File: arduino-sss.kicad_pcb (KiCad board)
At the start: 2 copper layers, 68.6 x 53.3 mm, 47 parts, among them J1 Conn_01x03_Male, J2 Barrel_Jack_Switch, J3 DB9_Male, J4 Conn_01x02_Male, J5 Conn_02x03_Odd_Even, P1 Power, P2 Analog, P3 Digital, P4 Digital, P5 CONN_01X01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

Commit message: update
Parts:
- J3: value DB9_Male -> DB9_Female_MountingHoles; footprint Connector_Dsub:DSUB-9_Male_Horizontal_P2.77x2.54mm_EdgePinOffset9.40mm -> Connector_Dsub:DSUB-9_Female_Horizontal_P2.77x2.84mm_EdgePinOffset4.94mm_Housed_MountingHolesOffset7.48mm
- moved J1 66.7 mm to (113.4, 111.4), turned to 90 degrees
- moved SW1 56.1 mm to (165.6, 96.9), turned to 180 degrees
- moved C1 53.9 mm to (121.5, 104.9), turned to 270 degrees
- moved R7 50.8 mm to (131.6, 87.2), turned to 0 degrees
- moved C3 46.1 mm to (129.5, 109.5), turned to 0 degrees
- moved R9 42.7 mm to (167.7, 110.6), turned to 270 degrees
- moved C9 38.8 mm to (151.6, 119.8), turned to 0 degrees
- moved R2 38.1 mm to (138.9, 110.6), turned to 0 degrees
- moved R11 37.6 mm to (172.0, 110.6), turned to 270 degrees
- moved J4 35.0 mm to (169.2, 94.0)
- moved C2 34.6 mm to (120.8, 101.2), turned to 0 degrees
- moved D2 33.0 mm to (138.9, 120.1), turned to 0 degrees
- moved D3 32.8 mm to (138.9, 115.5), turned to 0 degrees
- moved R10 30.1 mm to (172.5, 79.5), turned to 270 degrees
- moved C4 22.6 mm to (126.6, 104.9), turned to 270 degrees
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
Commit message: ready to fab
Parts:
- AUTO RESET: renamed from J4
- renumbered J5 to ICSP, D7 to L, D6 to ON, D5 to RX, J1 to SERIAL, D4 to TX
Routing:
- net GNDD: track 0.00 -> 244.5 mm, vias 0 -> 32
- net +5V: track 0.00 -> 145.2 mm
- net /A5(SCL): track 0.00 -> 102.1 mm
- net /A4(SDA): track 0.00 -> 95.3 mm
- net Net-(D3-Pad1): track 0.00 -> 93.8 mm, vias 0 -> 1
- net /Reset: track 0.00 -> 89.2 mm
- net /11(**/MOSI): track 0.00 -> 87.9 mm, vias 0 -> 1
- net /12(MISO): track 0.00 -> 85.7 mm
- net /13(SCK): track 0.00 -> 75.4 mm
- net /0(Rx): track 0.00 -> 74.4 mm
- net Net-(J1-Pad2): track 0.00 -> 74.3 mm
- net Net-(C5-Pad2): track 0.00 -> 67.6 mm
- net Net-(Q2-Pad2): track 0.00 -> 64.2 mm
- net Net-(D2-Pad1): track 0.00 -> 60.4 mm
- net Net-(Q1-Pad1): track 0.00 -> 58.7 mm, vias 0 -> 1
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- added copper zone on B.Cu, net GNDD
- added copper zone on F.Cu, net GNDD

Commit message: add version info
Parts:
- added G2: LOGO, LOGO, B.Cu at (150.4, 84.6)
- added REF**: KiCad-Logo2_5mm_SilkScreen, Symbol:KiCad-Logo2_5mm_SilkScreen, B.Cu at (167.8, 115.4)
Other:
- board text added: "Created by Yang Le Based on Arduino S3v3 R2 10/2019 Ver 0.5"

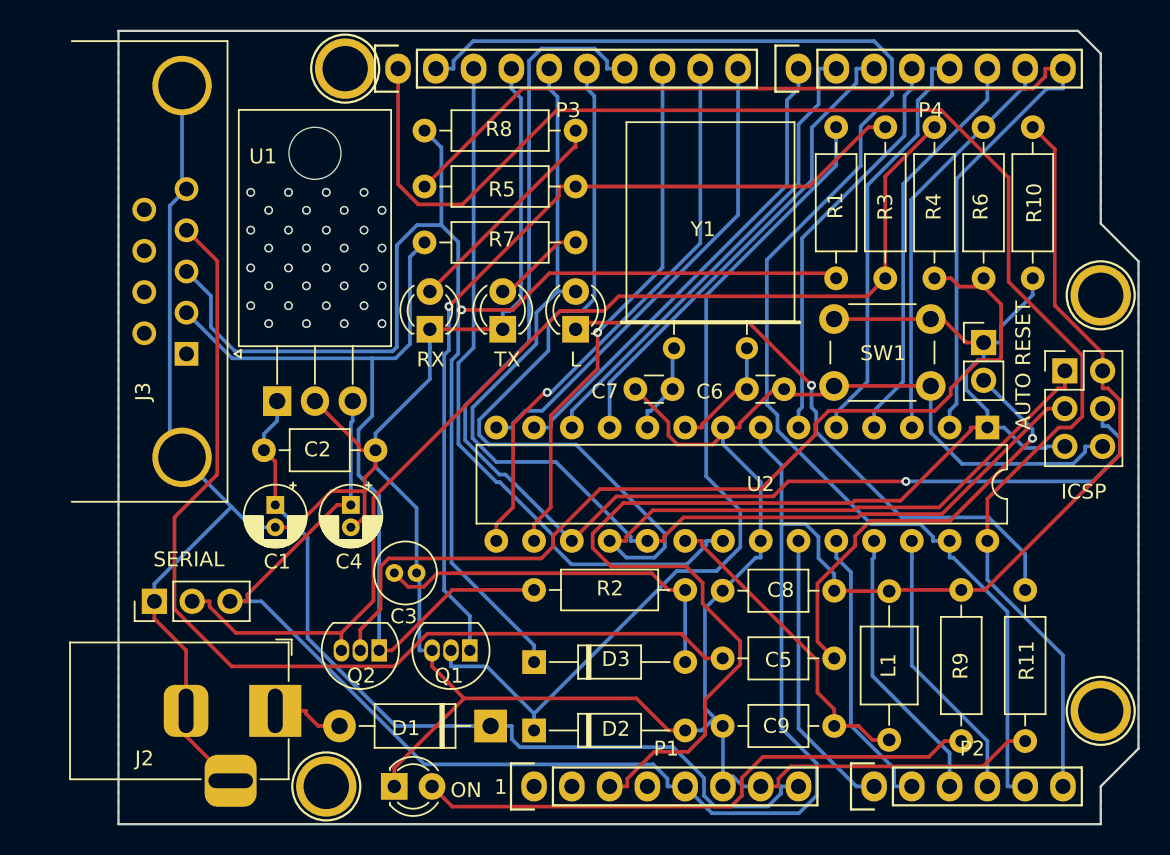
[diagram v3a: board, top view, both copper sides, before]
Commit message: update according to Real BOM
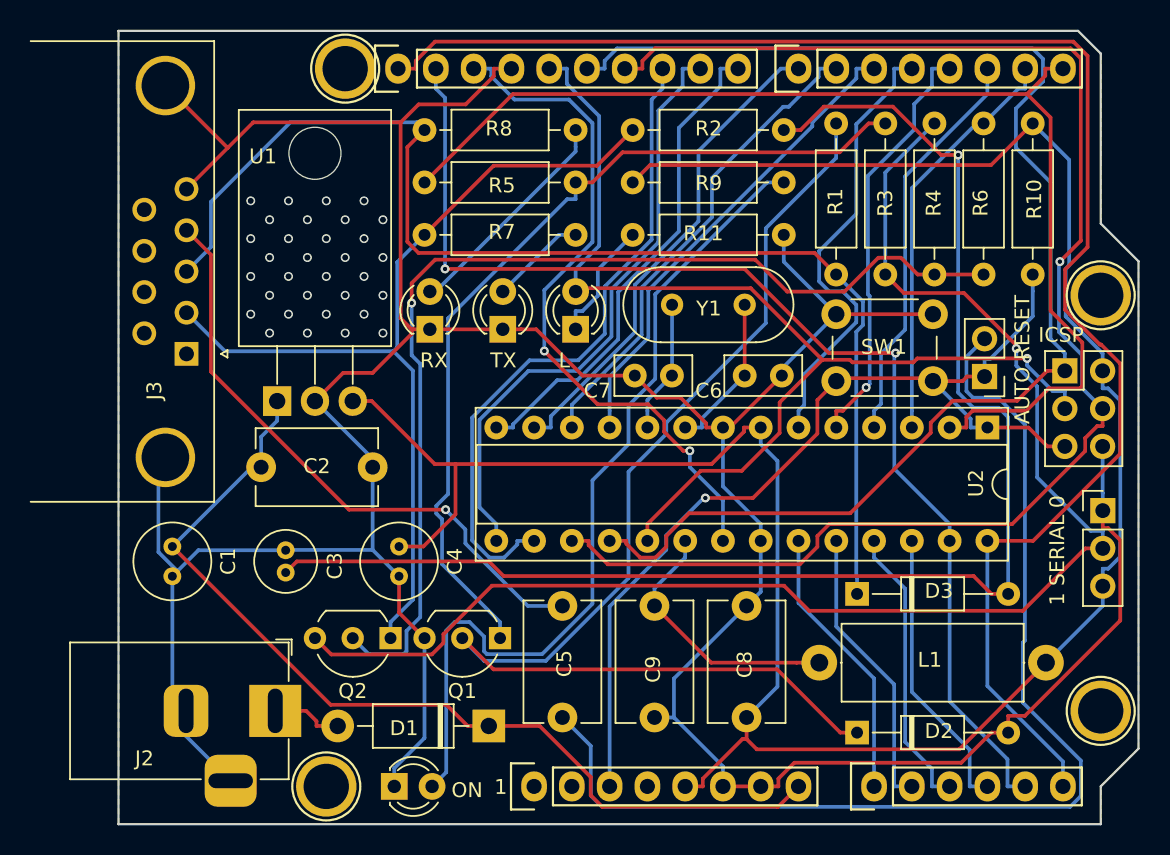
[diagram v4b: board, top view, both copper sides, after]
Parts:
- C1, C4: footprint Capacitor_THT:CP_Radial_D4.0mm_P1.50mm -> Capacitor_THT:C_Radial_D5.0mm_H7.0mm_P2.00mm
- C2, C5, C8, C9: footprint Capacitor_THT:C_Axial_L3.8mm_D2.6mm_P7.50mm_Horizontal -> Capacitor_THT:C_Disc_D8.0mm_W5.0mm_P7.50mm
- C3: footprint Capacitor_THT:C_Radial_D4.0mm_H5.0mm_P1.50mm -> Capacitor_THT:C_Radial_D4.0mm_H7.0mm_P1.50mm
- C6, C7: footprint Capacitor_THT:C_Disc_D3.0mm_W1.6mm_P2.50mm -> Capacitor_THT:C_Disc_D5.0mm_W2.5mm_P2.50mm
- D6: renamed from ON; value POWER -> ON
- D7: renamed from L; value LED13 -> L
- J1: renamed from SERIAL; value Conn_01x03_Male -> 1 SERIAL 0
- J3: footprint Connector_Dsub:DSUB-9_Female_Horizontal_P2.77x2.84mm_EdgePinOffset4.94mm_Housed_MountingHolesOffset7.48mm -> Connector_Dsub:DSUB-9_Female_Horizontal_P2.77x2.84mm_EdgePinOffset7.70mm_Housed_MountingHolesOffset9.12mm
- J4: renamed from AUTO RESET; value Conn_01x02_Male -> AUTO RESET
- J5: renamed from ICSP; value Conn_02x03_Odd_Even -> ICSP
- L1: footprint Inductor_THT:L_Axial_L5.0mm_D3.6mm_P10.00mm_Horizontal_Murata_BL01RN1A2A2 -> Inductor_THT:L_Axial_L12.0mm_D5.0mm_P15.24mm_Horizontal_Fastron_MISC
- Q1, Q2: footprint Package_TO_SOT_THT:TO-92_Inline -> Package_TO_SOT_THT:TO-92_Inline_Wide
- U2: footprint Package_DIP:DIP-28_W7.62mm -> Package_DIP:DIP-28_W7.62mm_Socket
- Y1: footprint Crystal:Crystal_HC18-U_Horizontal -> Crystal:Crystal_HC49-4H_Vertical
- moved J1 64.1 mm to (177.2, 105.3), turned to 0 degrees
- moved R11 35.6 mm to (145.6, 86.7), turned to 0 degrees
- moved R9 35.2 mm to (145.6, 83.2), turned to 0 degrees
- moved R2 31.6 mm to (145.6, 79.7)
- moved D3 22.2 mm to (160.7, 110.9)
- moved D2 21.7 mm to (160.7, 120.2)
- moved C5 18.7 mm to (140.8, 119.2), turned to 90 degrees
- moved G2 13.6 mm to (164.0, 84.2)
- moved L1 11.6 mm to (173.4, 115.5), turned to 180 degrees
- moved SW1 7.98 mm to (159.3, 92.1), turned to 0 degrees
- moved C1 7.46 mm to (114.6, 107.7)
- moved C3 7.30 mm to (122.2, 109.4), turned to 90 degrees
- moved C9 4.62 mm to (147.0, 119.2), turned to 90 degrees
- moved C4 4.28 mm to (129.9, 107.7)
- moved Y1 2.93 mm to (153.1, 91.4)
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- renumbered TX to D4, RX to D5
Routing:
- net Net-(C3-Pad1): track 25.6 -> 95.4 mm, vias 0 -> 1
- net Net-(C5-Pad1): track 29.6 -> 75.1 mm, vias 1 -> 0
- net Net-(D7-Pad1): track 40.9 -> 8.21 mm, vias 1 -> 0
- net Net-(C5-Pad2): track 67.6 -> 40.9 mm, vias 0 -> 1
- net /Reset: track 89.2 -> 65.2 mm, vias 0 -> 1
- net Net-(J1-Pad2): track 74.3 -> 97.0 mm, vias 0 -> 1
- net Net-(D6-Pad2): track 38.7 -> 58.1 mm
- net Net-(D2-Pad1): track 60.4 -> 79.7 mm
- net /A4(SDA): track 95.3 -> 79.9 mm, vias 0 -> 2
- net +5V: track 145.2 -> 159.2 mm
- net /11(**/MOSI): track 87.9 -> 99.6 mm
- net Net-(D3-Pad1): track 93.8 -> 82.3 mm, vias 1 -> 0
- net /10(**/SS): track 35.3 -> 44.2 mm, vias 1 -> 0
- net Net-(Q2-Pad2): track 64.2 -> 70.9 mm, vias 0 -> 1
- net /Vin: track 57.3 -> 63.7 mm
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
